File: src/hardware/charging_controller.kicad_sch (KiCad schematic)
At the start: 14 parts

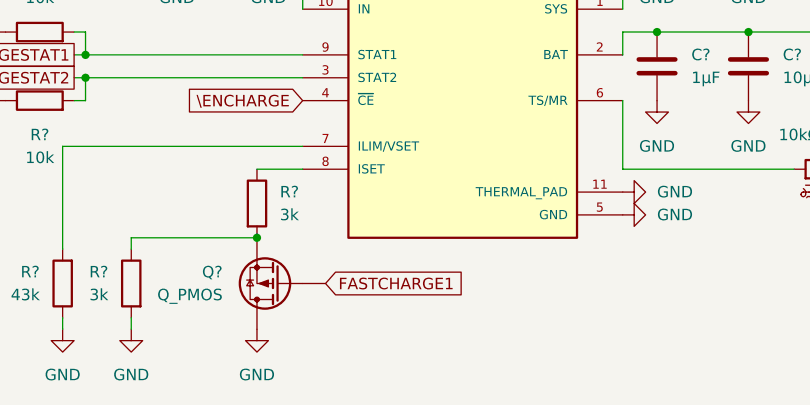
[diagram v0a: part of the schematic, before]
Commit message: Removed 4.5V page. 4.5V will come from the charging controller directly
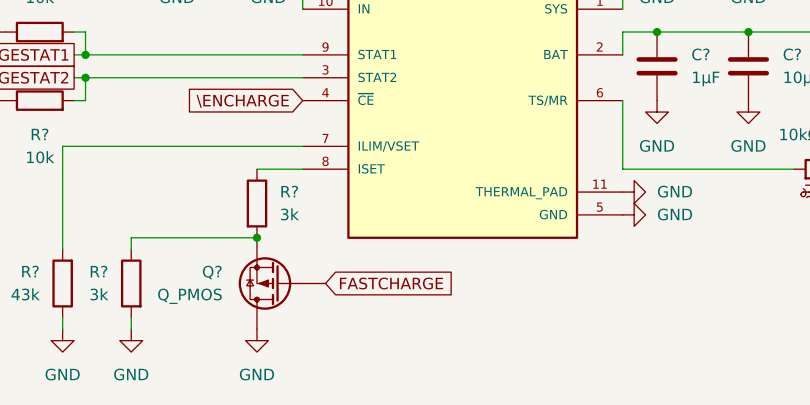
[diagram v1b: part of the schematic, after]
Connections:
- net FASTCHARGE1 renamed FASTCHARGE
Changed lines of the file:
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@@
 		)
 	)
-	(global_label "FASTCHARGE1"
+	(global_label "FASTCHARGE"
 		(shape input)
 		(at 132.08 119.38 0)
@@
 		)
 		(property "Intersheetrefs" "${INTERSHEET_REFS}"
-			(at 148.0071 119.38 0)
+			(at 146.7976 119.38 0)
 			(effects
 				(font

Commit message: Changed power symboles
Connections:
- net VIN: now reaches C?.2, C?.2, U?.10 (IN)
- net +4V5: now reaches C?.2, C?.2, U?.1 (SYS)
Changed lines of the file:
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@@
+	)
+	(junction
+		(at 172.72 74.93)
+		(diameter 0)
+		(color 0 0 0 0)
+	)
+	(junction
+		(at 168.91 74.93)
+		(diameter 0)
+		(color 0 0 0 0)
 	)
 	(junction
@@
 	)
 	(junction
-		(at 168.91 74.93)
-		(diameter 0)
-		(color 0 0 0 0)
-	)
-	(junction
 		(at 179.07 91.44)
 		(diameter 0)
@@
 	)
 	(junction
+		(at 179.07 74.93)
+		(diameter 0)
+		(color 0 0 0 0)
+	)
+	(junction
 		(at 105.41 96.52)
 		(diameter 0)
@@
 	(wire
 		(pts
+			(xy 172.72 74.93) (xy 179.07 74.93)
+		)
+		(stroke
+			(width 0)
+			(type default)
+		)
+	)
+	(wire
+		(pts
 			(xy 165.1 91.44) (xy 165.1 93.98)
 		)
@@
 	(wire
 		(pts
-			(xy 168.91 74.93) (xy 179.07 74.93)
+			(xy 168.91 74.93) (xy 172.72 74.93)
 		)
 		(stroke
@@
 	)
 	(symbol
+		(lib_id "power:LINE")
+		(at 190.5 74.93 0)
+		(unit 1)
+		(exclude_from_sim no)
+		(in_bom yes)
+		(on_board yes)
+		(dnp no)
+		(fields_autoplaced yes)
+		(property "Reference" "#PWR0357"
+			(at 190.5 78.74 0)
+			(effects
+				(font
+					(size 1.27 1.27)
+				)
+				(hide yes)
+			)
+		)
+		(property "Value" "VBAT"
+			(at 190.5 69.85 0)
+			(effects
+				(font
+					(size 1.27 1.27)
+				)
+			)
+		)
+		(property "Footprint" ""
+			(at 190.5 74.93 0)
+			(effects
+				(font
+					(size 1.27 1.27)
+				)
+				(hide yes)
+			)
+		)
+		(property "Datasheet" ""
+			(at 190.5 74.93 0)
+			(effects
+				(font
+					(size 1.27 1.27)
+				)
+				(hide yes)
+			)
+		)
+		(property "Description" "Power symbol creates a global label with name \"LINE\""
+			(at 190.5 74.93 0)
+			(effects
+				(font
+					(size 1.27 1.27)
+				)
+				(hide yes)
+			)
+		)
+		(pin "1"
+		)
+		(instances
+			(project "raywatch"
+				(path "/7b654ee8-2a53-4d39-8b7d-32c7bb3cb0ed/6e6a70ea-4db2-4b59-a2d7-c468f9b8b5a6/e601ae13-e808-457e-9f3e-dffc594463cc"
+					(reference "#PWR0357")
+					(unit 1)
+				)
+			)
+		)
+	)
+	(symbol
 		(lib_id "power:GND")
 		(at 179.07 82.55 0)
@@
 	)
 	(symbol
-		(lib_id "power:+5V")
-		(at 190.5 74.93 0)
-		(unit 1)
-		(exclude_from_sim no)
-		(in_bom yes)
-		(on_board yes)
-		(dnp no)
-		(fields_autoplaced yes)
-		(property "Reference" "#PWR0358"
-			(at 190.5 78.74 0)
-			(effects
-				(font
-					(size 1.27 1.27)
-				)
-				(hide yes)
-			)
-		)
-		(property "Value" "VBAT"
-			(at 190.5 69.85 0)
-			(effects
-				(font
-					(size 1.27 1.27)
-				)
-			)
-		)
-		(property "Footprint" ""
-			(at 190.5 74.93 0)
-			(effects
-				(font
-					(size 1.27 1.27)
-				)
-				(hide yes)
-			)
-		)
-		(property "Datasheet" ""
-			(at 190.5 74.93 0)
-			(effects
-				(font
-					(size 1.27 1.27)
-				)
-				(hide yes)
-			)
-		)
-		(property "Description" "Power symbol creates a global label with name \"+5V\""
-			(at 190.5 74.93 0)
-			(effects
-				(font
-					(size 1.27 1.27)
-				)
-				(hide yes)
-			)
-		)
-		(pin "1"
-		)
-		(instances
-			(project "raywatch"
-				(path "/7b654ee8-2a53-4d39-8b7d-32c7bb3cb0ed/6e6a70ea-4db2-4b59-a2d7-c468f9b8b5a6/e601ae13-e808-457e-9f3e-dffc594463cc"
-					(reference "#PWR0358")
-					(unit 1)
-				)
-			)
-		)
-	)
-	(symbol
 		(lib_id "power:GND")
 		(at 124.46 124.46 0)
@@
 				(path "/7b654ee8-2a53-4d39-8b7d-32c7bb3cb0ed/6e6a70ea-4db2-4b59-a2d7-c468f9b8b5a6/e601ae13-e808-457e-9f3e-dffc594463cc"
 					(reference "#PWR0352")
+					(unit 1)
+				)
+			)
+		)
+	)
+	(symbol
+		(lib_id "power:+1V1")
+		(at 172.72 74.93 0)
+		(unit 1)
+		(exclude_from_sim no)
+		(in_bom yes)
+		(on_board yes)
+		(dnp no)
+		(fields_autoplaced yes)
+		(property "Reference" "#PWR0372"
+			(at 172.72 78.74 0)
+			(effects
+				(font
+					(size 1.27 1.27)
+				)
+				(hide yes)
+			)
+		)
+		(property "Value" "+4V5"
+			(at 172.72 69.85 0)
+			(effects
+				(font
+					(size 1.27 1.27)
+				)
+			)
+		)
+		(property "Footprint" ""
+			(at 172.72 74.93 0)
+			(effects
+				(font
+					(size 1.27 1.27)
+				)
+				(hide yes)
+			)
+		)
+		(property "Datasheet" ""
+			(at 172.72 74.93 0)
+			(effects
+				(font
+					(size 1.27 1.27)
+				)
+				(hide yes)
+			)
+		)
+		(property "Description" "Power symbol creates a global label with name \"+1V1\""
+			(at 172.72 74.93 0)
+			(effects
+				(font
+					(size 1.27 1.27)
+				)
+				(hide yes)
+			)
+		)
+		(pin "1"
+		)
+		(instances
+			(project "raywatch"
+				(path "/7b654ee8-2a53-4d39-8b7d-32c7bb3cb0ed/6e6a70ea-4db2-4b59-a2d7-c468f9b8b5a6/e601ae13-e808-457e-9f3e-dffc594463cc"
+					(reference "#PWR0372")
 					(unit 1)
 				)
@@
 	)
 	(symbol
+		(lib_id "power:LINE")
+		(at 115.57 74.93 0)
+		(unit 1)
+		(exclude_from_sim no)
+		(in_bom yes)
+		(on_board yes)
+		(dnp no)
+		(fields_autoplaced yes)
+		(property "Reference" "#PWR0367"
+			(at 115.57 78.74 0)
+			(effects
+				(font
+					(size 1.27 1.27)
+				)
+				(hide yes)
+			)
+		)
+		(property "Value" "VIN"
+			(at 115.57 69.85 0)
+			(effects
+				(font
+					(size 1.27 1.27)
+				)
+			)
+		)
+		(property "Footprint" ""
+			(at 115.57 74.93 0)
+			(effects
+				(font
+					(size 1.27 1.27)
+				)
+				(hide yes)
+			)
+		)
+		(property "Datasheet" ""
+			(at 115.57 74.93 0)
+			(effects
+				(font
+					(size 1.27 1.27)
+				)
+				(hide yes)
+			)
+		)
+		(property "Description" "Power symbol creates a global label with name \"LINE\""
+			(at 115.57 74.93 0)
+			(effects
+				(font
+					(size 1.27 1.27)
+				)
+				(hide yes)
+			)
+		)
+		(pin "1"
+		)
+		(instances
+			(project "raywatch"
+				(path "/7b654ee8-2a53-4d39-8b7d-32c7bb3cb0ed/6e6a70ea-4db2-4b59-a2d7-c468f9b8b5a6/e601ae13-e808-457e-9f3e-dffc594463cc"
+					(reference "#PWR0367")
+					(unit 1)
+				)
+			)
+		)
+	)
+	(symbol
 		(lib_id "Device:C")
 		(at 179.07 78.74 180)
@@
 	)
 	(symbol
+		(lib_id "power:LINE")
+		(at 179.07 74.93 0)
+		(unit 1)
+		(exclude_from_sim no)
+		(in_bom yes)
+		(on_board yes)
+		(dnp no)
+		(fields_autoplaced yes)
+		(property "Reference" "#PWR0358"
+			(at 179.07 78.74 0)
+			(effects
+				(font
+					(size 1.27 1.27)
+				)
+				(hide yes)
+			)
+		)
+		(property "Value" "VSYS"
+			(at 179.07 69.85 0)
+			(effects
+				(font
+					(size 1.27 1.27)
+				)
+			)
+		)
+		(property "Footprint" ""
+			(at 179.07 74.93 0)
+			(effects
+				(font
+					(size 1.27 1.27)
+				)
+				(hide yes)
+			)
+		)
+		(property "Datasheet" ""
+			(at 179.07 74.93 0)
+			(effects
+				(font
+					(size 1.27 1.27)
+				)
+				(hide yes)
+			)
+		)
+		(property "Description" "Power symbol creates a global label with name \"LINE\""
+			(at 179.07 74.93 0)
+			(effects
+				(font
+					(size 1.27 1.27)
+				)
+				(hide yes)
+			)
+		)
+		(pin "1"
+		)
+		(instances
+			(project "raywatch"
+				(path "/7b654ee8-2a53-4d39-8b7d-32c7bb3cb0ed/6e6a70ea-4db2-4b59-a2d7-c468f9b8b5a6/e601ae13-e808-457e-9f3e-dffc594463cc"
+					(reference "#PWR0358")
+					(unit 1)
+				)
+			)
+		)
+	)
+	(symbol
 		(lib_id "power:GND")
 		(at 165.1 109.22 90)
@@
 					(unit 1)
 				)
-			)
-		)
-	)
-	(symbol
-		(lib_id "power:PWR_FLAG")
-		(at 115.57 74.93 0)
-		(unit 1)
-		(exclude_from_sim no)
-		(in_bom yes)
-		(on_board yes)
-		(dnp no)
-		(fields_autoplaced yes)
-		(property "Reference" "#FLG03"
-			(at 115.57 73.025 0)
-			(effects
-				(font
-					(size 1.27 1.27)
-				)
-				(hide yes)
-			)
-		)
-		(property "Value" "PWR_FLAG"
-			(at 115.57 69.85 0)
-			(effects
-				(font
-					(size 1.27 1.27)
-				)
-			)
-		)
-		(property "Footprint" ""
-			(at 115.57 74.93 0)
-			(effects
-				(font
-					(size 1.27 1.27)
-				)
-				(hide yes)
-			)
-		)
-		(property "Datasheet" "~"
-			(at 115.57 74.93 0)
-			(effects
-				(font
-					(size 1.27 1.27)
-				)
-				(hide yes)
-			)
-		)
-		(property "Description" "Special symbol for telling ERC where power comes from"
-			(at 115.57 74.93 0)
-			(effects
-				(font
-					(size 1.27 1.27)
-				)
-				(hide yes)
-			)
-		)
-		(pin "1"
-		)
-		(instances
-			(project "raywatch"
-				(path "/7b654ee8-2a53-4d39-8b7d-32c7bb3cb0ed/6e6a70ea-4db2-4b59-a2d7-c468f9b8b5a6/e601ae13-e808-457e-9f3e-dffc594463cc"
-					(reference "#FLG03")
-					(unit 1)
-				)

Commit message: Added Accelerometer Clock; Cleanup & Fixes
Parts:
- R? (x2): value 10k -> 10kΩ
- R? (x2): value 3k -> 2.2kΩ
- R?: value 43k -> 43kΩ
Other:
- moved on the sheet: R?
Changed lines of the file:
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@@
 	(wire
 		(pts
-			(xy 110.49 124.46) (xy 110.49 123.19)
+			(xy 101.6 124.46) (xy 101.6 123.19)
 		)
 		(stroke
@@
 	(wire
 		(pts
-			(xy 110.49 115.57) (xy 110.49 114.3)
+			(xy 101.6 115.57) (xy 101.6 114.3)
 		)
 		(stroke
@@
 	(wire
 		(pts
-			(xy 102.87 115.57) (xy 102.87 104.14)
+			(xy 96.52 115.57) (xy 96.52 104.14)
 		)
 		(stroke
@@
 	(wire
 		(pts
-			(xy 102.87 104.14) (xy 129.54 104.14)
+			(xy 96.52 104.14) (xy 129.54 104.14)
 		)
 		(stroke
@@
 	(wire
 		(pts
-			(xy 110.49 114.3) (xy 124.46 114.3)
-		)
-		(stroke
-			(width 0)
-			(type default)
-		)
-	)
-	(wire
-		(pts
-			(xy 102.87 124.46) (xy 102.87 123.19)
+			(xy 101.6 114.3) (xy 124.46 114.3)
+		)
+		(stroke
+			(width 0)
+			(type default)
+		)
+	)
+	(wire
+		(pts
+			(xy 96.52 124.46) (xy 96.52 123.19)
 		)
 		(stroke
@@
 			)
 		)
-		(property "Value" "10k"
+		(property "Value" "10kΩ"
 			(at 100.33 87.63 90)
 			(effects
@@
 			)
 		)
-		(property "Value" "10k"
+		(property "Value" "10kΩ"
 			(at 100.33 105.41 90)
 			(effects
@@
 	(symbol
 		(lib_id "Device:R")
-		(at 110.49 119.38 0)
+		(at 101.6 119.38 0)
 		(mirror y)
 		(unit 1)
@@
 		(fields_autoplaced yes)
 		(property "Reference" "R?"
-			(at 107.95 118.1099 0)
-			(effects
-				(font
-					(size 1.27 1.27)
-				)
-				(justify left)
-			)
-		)
-		(property "Value" "3k"
-			(at 107.95 120.6499 0)
-			(effects
-				(font
-					(size 1.27 1.27)
-				)
-				(justify left)
-			)
-		)
-		(property "Footprint" ""
-			(at 112.268 119.38 90)
+			(at 104.14 118.1099 0)
+			(effects
+				(font
+					(size 1.27 1.27)
+				)
+				(justify right)
+			)
+		)
+		(property "Value" "2.2kΩ"
+			(at 104.14 120.6499 0)
+			(effects
+				(font
+					(size 1.27 1.27)
+				)
+				(justify right)
+			)
+		)
+		(property "Footprint" ""
+			(at 103.378 119.38 90)
 			(effects
 				(font
@@
 		)
 		(property "Datasheet" "~"
-			(at 110.49 119.38 0)
+			(at 101.6 119.38 0)
 			(effects
 				(font
@@
 		)
 		(property "Description" "Resistor"
-			(at 110.49 119.38 0)
+			(at 101.6 119.38 0)
 			(effects
 				(font
@@
 	(symbol
 		(lib_id "Device:R")
-		(at 102.87 119.38 180)
+		(at 96.52 119.38 180)
 		(unit 1)
 		(exclude_from_sim no)
@@
 		(fields_autoplaced yes)
 		(property "Reference" "R?"
-			(at 100.33 118.1099 0)
+			(at 93.98 118.1099 0)
 			(effects
 				(font
@@
 			)
 		)
-		(property "Value" "43k"
-			(at 100.33 120.6499 0)
+		(property "Value" "43kΩ"
+			(at 93.98 120.6499 0)
 			(effects
 				(font
@@
 		)
 		(property "Footprint" ""
-			(at 104.648 119.38 90)
+			(at 98.298 119.38 90)
 			(effects
 				(font
@@
 		)
 		(property "Datasheet" "~"
-			(at 102.87 119.38 0)
+			(at 96.52 119.38 0)
 			(effects
 				(font
@@
 		)
 		(property "Description" "Resistor"
-			(at 102.87 119.38 0)
+			(at 96.52 119.38 0)
 			(effects
 				(font
@@
 	(symbol
 		(lib_id "power:GND")
-		(at 110.49 124.46 0)
+		(at 101.6 124.46 0)
 		(unit 1)
 		(exclude_from_sim no)
@@
 		(fields_autoplaced yes)
 		(property "Reference" "#PWR0362"
-			(at 110.49 130.81 0)
+			(at 101.6 130.81 0)
 			(effects
 				(font
@@
 		)
 		(property "Value" "GND"
-			(at 110.49 129.54 0)
-			(effects
-				(font
-					(size 1.27 1.27)
-				)
-			)
-		)
-		(property "Footprint" ""
-			(at 110.49 124.46 0)
+			(at 101.6 129.54 0)
+			(effects
+				(font
+					(size 1.27 1.27)
+				)
+			)
+		)
+		(property "Footprint" ""
+			(at 101.6 124.46 0)
 			(effects
 				(font
@@
 		)
 		(property "Datasheet" ""
-			(at 110.49 124.46 0)
+			(at 101.6 124.46 0)
 			(effects
 				(font
@@
 		)
 		(property "Description" "Power symbol creates a global label with name \"GND\" , ground"
-			(at 110.49 124.46 0)
+			(at 101.6 124.46 0)
 			(effects
 				(font
@@
 	(symbol
 		(lib_id "power:GND")
-		(at 102.87 124.46 0)
+		(at 96.52 124.46 0)
 		(unit 1)
 		(exclude_from_sim no)
@@
 		(fields_autoplaced yes)
 		(property "Reference" "#PWR0364"
-			(at 102.87 130.81 0)
+			(at 96.52 130.81 0)
 			(effects
 				(font
@@
 		)
 		(property "Value" "GND"
-			(at 102.87 129.54 0)
-			(effects
-				(font
-					(size 1.27 1.27)
-				)
-			)
-		)
-		(property "Footprint" ""
-			(at 102.87 124.46 0)
+			(at 96.52 129.54 0)
+			(effects
+				(font
+					(size 1.27 1.27)
+				)
+			)
+		)
+		(property "Footprint" ""
+			(at 96.52 124.46 0)
 			(effects
 				(font
@@
 		)
 		(property "Datasheet" ""
-			(at 102.87 124.46 0)
+			(at 96.52 124.46 0)
 			(effects
 				(font
@@
 		)
 		(property "Description" "Power symbol creates a global label with name \"GND\" , ground"
-			(at 102.87 124.46 0)
+			(at 96.52 124.46 0)
 			(effects
 				(font
@@
 			)
 		)
-		(property "Value" "3k"
+		(property "Value" "2.2kΩ"
 			(at 127 111.7599 0)
 			(effects

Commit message: Cleanup & Fixes; Added footprints; Removed Light sensors
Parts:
- removed Q?: Q_PMOS, symbol Device:Q_PMOS
- added U29, U31: TPS22916BYFPR, Project:IC_TPS22916BYFPR, symbol TPS22916BYFPR:TPS22916BYFPR
- C93, C94, C95, C96, C97, C98: renamed from C?; footprint (none) -> Capacitor_SMD:C_0603_1608Metric
- R42, R43, R44, R45, R46: renamed from R?; footprint (none) -> Resistor_SMD:R_0603_1608Metric
- U30: renamed from U?; footprint BQ25185DLHR:IC_BQ25185DLHR -> Project:IC_BQ25185DLHR
- gave numbers to parts that had none: 1
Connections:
- net +4V5: now also U31.A1 (VOUT); no longer C95.2, C97.2, U30.1 (SYS)
- net FASTCHARGE: now also U29.B2 (ON)
- net GND: now also U29.A1 (VOUT), U29.B1 (GND), U31.B1 (GND)
- net at R45.1, R46.2: now also U29.A2 (VIN)
- new net 4V5EN: U31.B2 (ON)
- new net VSYS: C95.2, C97.2, U30.1 (SYS), U31.A2 (VIN)

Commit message: Cleanup & Fixes; Changed GPIO; Added Camera; Added Microphone
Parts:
- renumbered C93 to C91, C94 to C92, C95 to C93, C96 to C94, C97 to C95, C98 to C96, R42 to R40, R43 to R41, R44 to R42, R45 to R43, R46 to R44

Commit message: Add Light Sensor and Proximity & Gesture Sensor; Changed GPIO
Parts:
- removed U31: TPS22916BYFPR, Project:IC_TPS22916BYFPR, symbol TPS22916BYFPR:TPS22916BYFPR
- renumbered R40 to R41, R41 to R42, R42 to R43, R43 to R44, R44 to R45, U29 to U30, U30 to U31
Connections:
- net VSYS is gone; now on net +4V5: C93.2, C95.2, U31.1 (SYS)

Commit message: Flattend hirachy
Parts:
- renumbered C91 to C76, C92 to C77, C93 to C78, C94 to C79, C95 to C80, C96 to C81, R41 to R39, R42 to R40, R43 to R41, R44 to R42, R45 to R43
